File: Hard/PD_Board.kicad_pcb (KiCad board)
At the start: 2 copper layers, 70 x 30 mm, 71 parts, among them J1 Micro_SD_Card_Det_Hirose_DM3AT, J2 KRC_Conn_SWD, J3 USB_B_Micro, J4 KRC_Conn_CAN, J5 Servo, U1 CY8C58xxLTI-LPxxx, U2 TPS561201, U3 NCV7342, U4 LPS22HB, Y1 24MHz

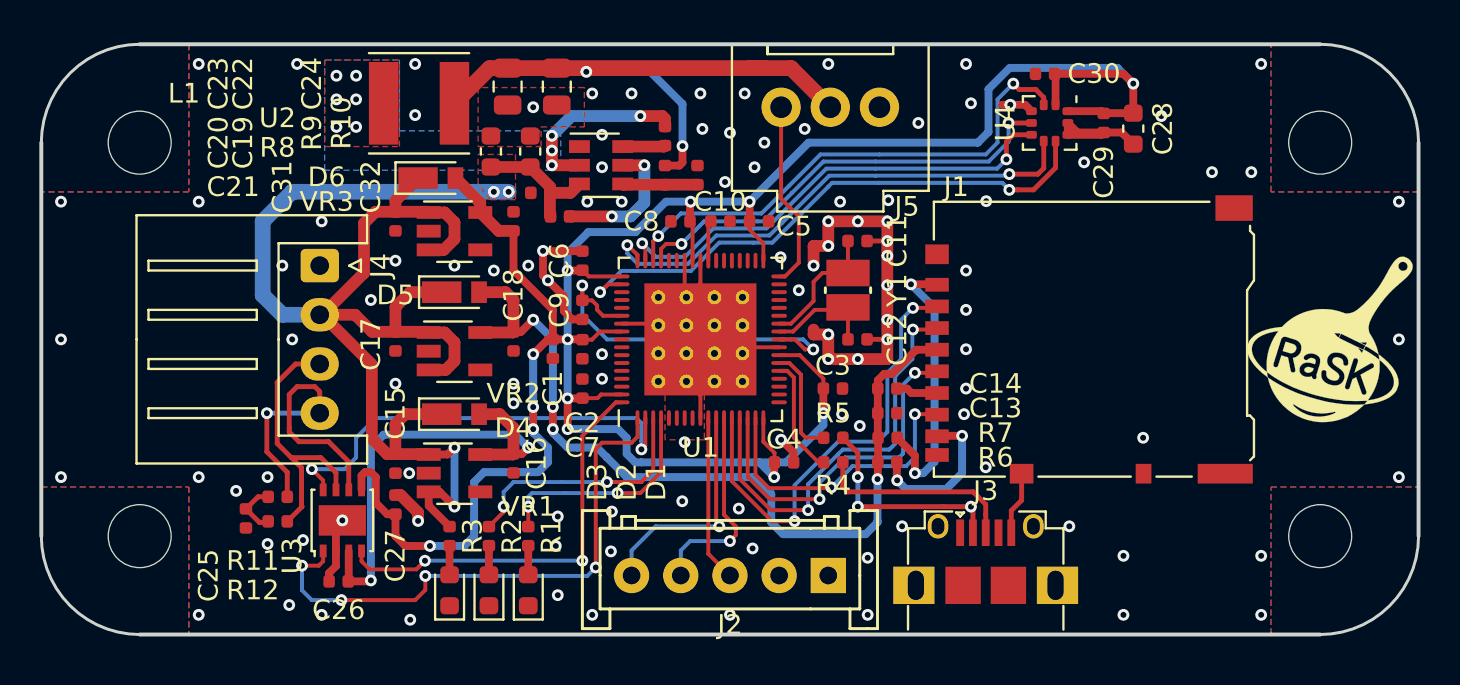
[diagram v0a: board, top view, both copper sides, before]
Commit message: [update] プルアップ抵抗ちゃんとしました
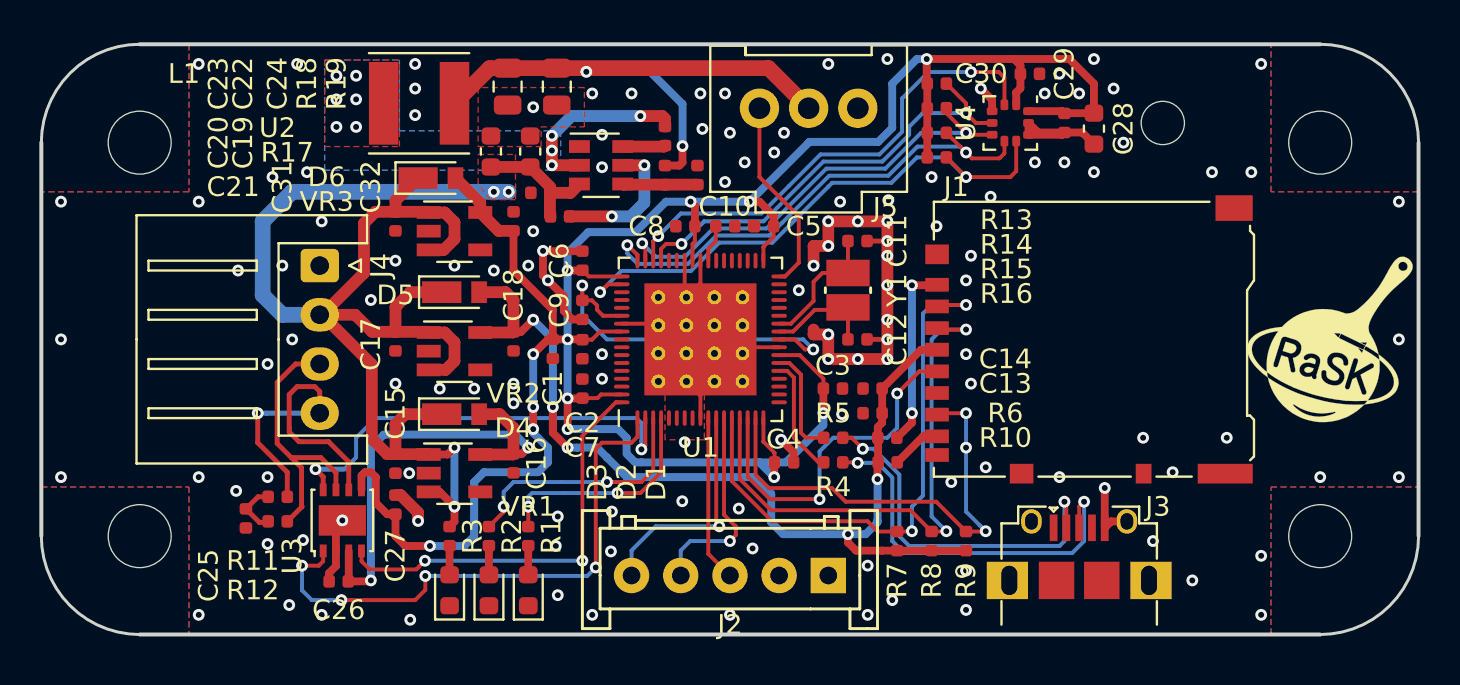
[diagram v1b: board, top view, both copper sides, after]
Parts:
- added R13: 22k, Resistor_SMD:R_0402_1005Metric, F.Cu at (160.5, 77.0)
- added R14: 22k, Resistor_SMD:R_0402_1005Metric, F.Cu at (160.5, 78.2)
- added R15: 22k, Resistor_SMD:R_0402_1005Metric, F.Cu at (160.5, 79.5)
- added R16: 22k, Resistor_SMD:R_0402_1005Metric, F.Cu at (160.5, 80.8)
- added R17: 10k, Resistor_SMD:R_0402_1005Metric, F.Cu at (141.4, 83.8)
- added R18: 68k, Resistor_SMD:R_0402_1005Metric, F.Cu at (146.7, 81.7)
- added R19: 10k, Resistor_SMD:R_0402_1005Metric, F.Cu at (148.3, 81.7)
- added REF**: MountingHole_2.2mm_M2, MountingHole:MountingHole_2.2mm_M2, F.Cu at (172.0, 79.0)
- R10, R8: value 10k -> 22k
- R6, R7: value 47k -> 22k
- R9: value 68k -> 22k
- moved R8 25.1 mm to (160.2, 100.2), turned to 90 degrees
- moved R9 24.1 mm to (162.0, 100.2)
- moved R10 17.5 mm to (158.0, 96.2), turned to 0 degrees
- moved R7 5.27 mm to (158.5, 100.2), turned to 90 degrees
- moved J3 4.76 mm to (167.8, 102.2)
- moved C28 2.00 mm to (168.5, 79.3)
- moved C29 2.00 mm to (167.0, 79.0)
- moved U4 2.00 mm to (164.2, 79.0)
- moved R6 1.25 mm to (158.0, 95.0)
- moved J5 1.10 mm to (156.5, 78.2)
- moved C30 0.76 mm to (165.2, 76.5), turned to 180 degrees
- moved C13 0.75 mm to (157.2, 93.8), turned to 180 degrees
- moved C14 0.75 mm to (157.2, 92.5), turned to 180 degrees
- moved C10 0.35 mm to (149.8, 84.2)
- moved C5 0.35 mm to (151.7, 84.2), turned to 180 degrees
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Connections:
- R10 pad 1: Net-(R10-Pad1) -> +3.3VP
- R10 pad 2: GND -> Net-(J1-Pad8)
- R6 pad 2: Net-(J1-Pad8) -> Net-(J1-Pad1)
- R7 pad 2: Net-(J1-Pad1) -> /SD_CS
- R8 pad 1: VCC -> +3.3VP
- R8 pad 2: Net-(R8-Pad2) -> /SD_MOSI
- R9 pad 1: Net-(R10-Pad1) -> +3.3VP
- R9 pad 2: +6V -> /SD_MISO
- U2 pad 4: Net-(R10-Pad1) -> Net-(R18-Pad1)
- U2 pad 5: Net-(R8-Pad2) -> Net-(R17-Pad2)
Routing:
- net Net-(J3-Pad3): track 10.3 -> 19.7 mm, vias 0 -> 2
- net /SD_MISO: track 15.2 -> 24.1 mm, vias 2 -> 3
- net Net-(J3-Pad2): track 10.9 -> 18.8 mm, vias 3 -> 2
- net +3.3VP: track 43.3 -> 50.6 mm, vias 4 -> 5
- net Net-(R8-Pad2): track 7.09 -> 0.00 mm, vias 2 -> 0
- net Net-(R17-Pad2): track 0.00 -> 7.09 mm, vias 0 -> 2
- net /SD_MOSI: track 21.3 -> 28.2 mm
- net /SD_CS: track 23.0 -> 28.6 mm
- net Net-(J1-Pad8): track 7.92 -> 2.57 mm, vias 2 -> 0
- net Net-(J1-Pad1): track 14.3 -> 9.35 mm
- net Net-(R18-Pad1): track 0.00 -> 3.81 mm
- net Net-(R10-Pad1): track 3.81 -> 0.00 mm
- net GND: track 58.4 -> 56.5 mm, vias 110 -> 128
- net +6V: track 32.5 -> 30.7 mm
- net /LPS_CLK: track 26.1 -> 24.9 mm
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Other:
- net class Default: clearance 0.1 -> 0.16
- rule trace_clearance: 0.1 -> 0.16

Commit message: [add] ガーバー出力
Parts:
- added REF**: KiCad-Logo2_5mm_SilkScreen, Symbol:KiCad-Logo2_5mm_SilkScreen, B.Cu at (164.0, 79.0)
- moved G*** 2.08 mm to (146.5, 93.5)

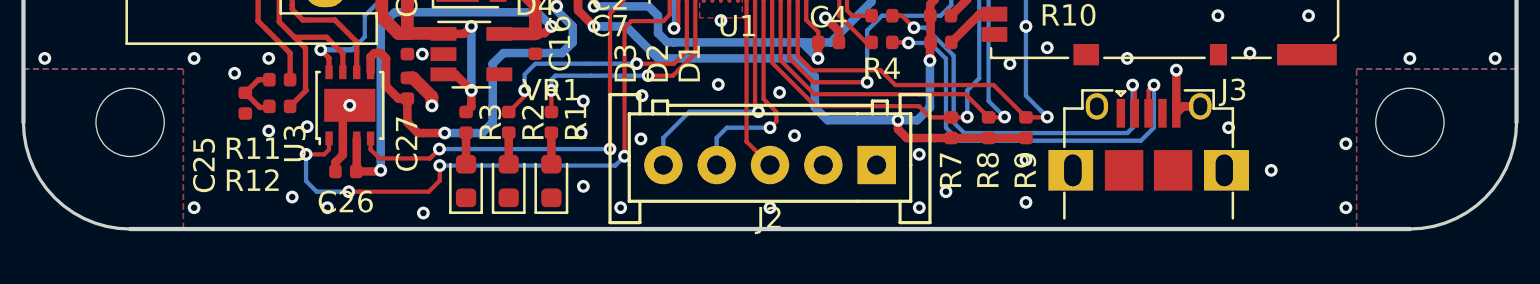
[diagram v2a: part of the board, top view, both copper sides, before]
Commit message: [add] USBに切り欠きを追加.ガーバー出力
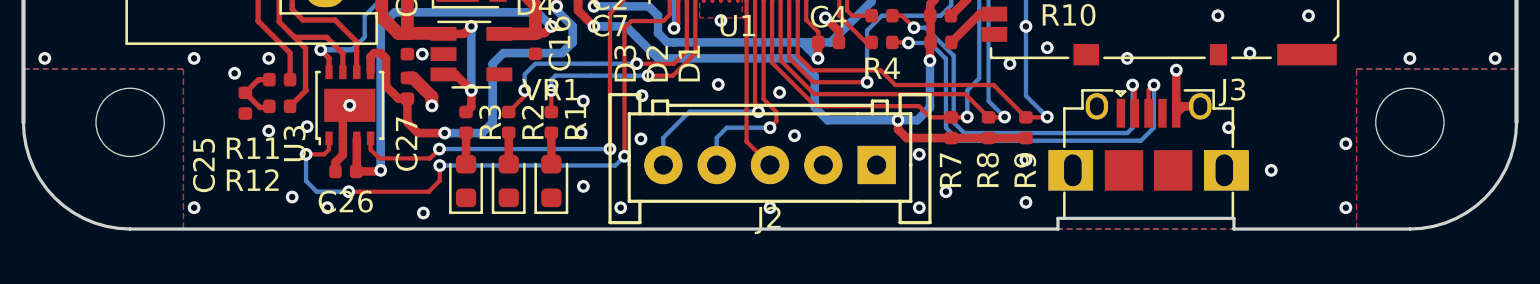
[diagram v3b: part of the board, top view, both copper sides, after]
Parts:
- added REF**: OSHW-Symbol_6.7x6mm_SilkScreen, Symbol:OSHW-Symbol_6.7x6mm_SilkScreen, B.Cu at (126.2, 101.2)
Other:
- outline, holes or cut-outs redrawn
